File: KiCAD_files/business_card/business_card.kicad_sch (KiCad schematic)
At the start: 80 parts, among them J1 USB_C_Receptacle_USB2.0_14P, J2 Conn_01x05_Pin, SW1 SW_Push, SW2 SW_Push, SW3 SW_Push, SW4 SW_Push, SW5 SW_Push, SW6 SW_Push, SW7 SW_Push, SW8 SW_MEC_5E, U1 STM32U073CCUx, U2 MCP1700x-300xxTT

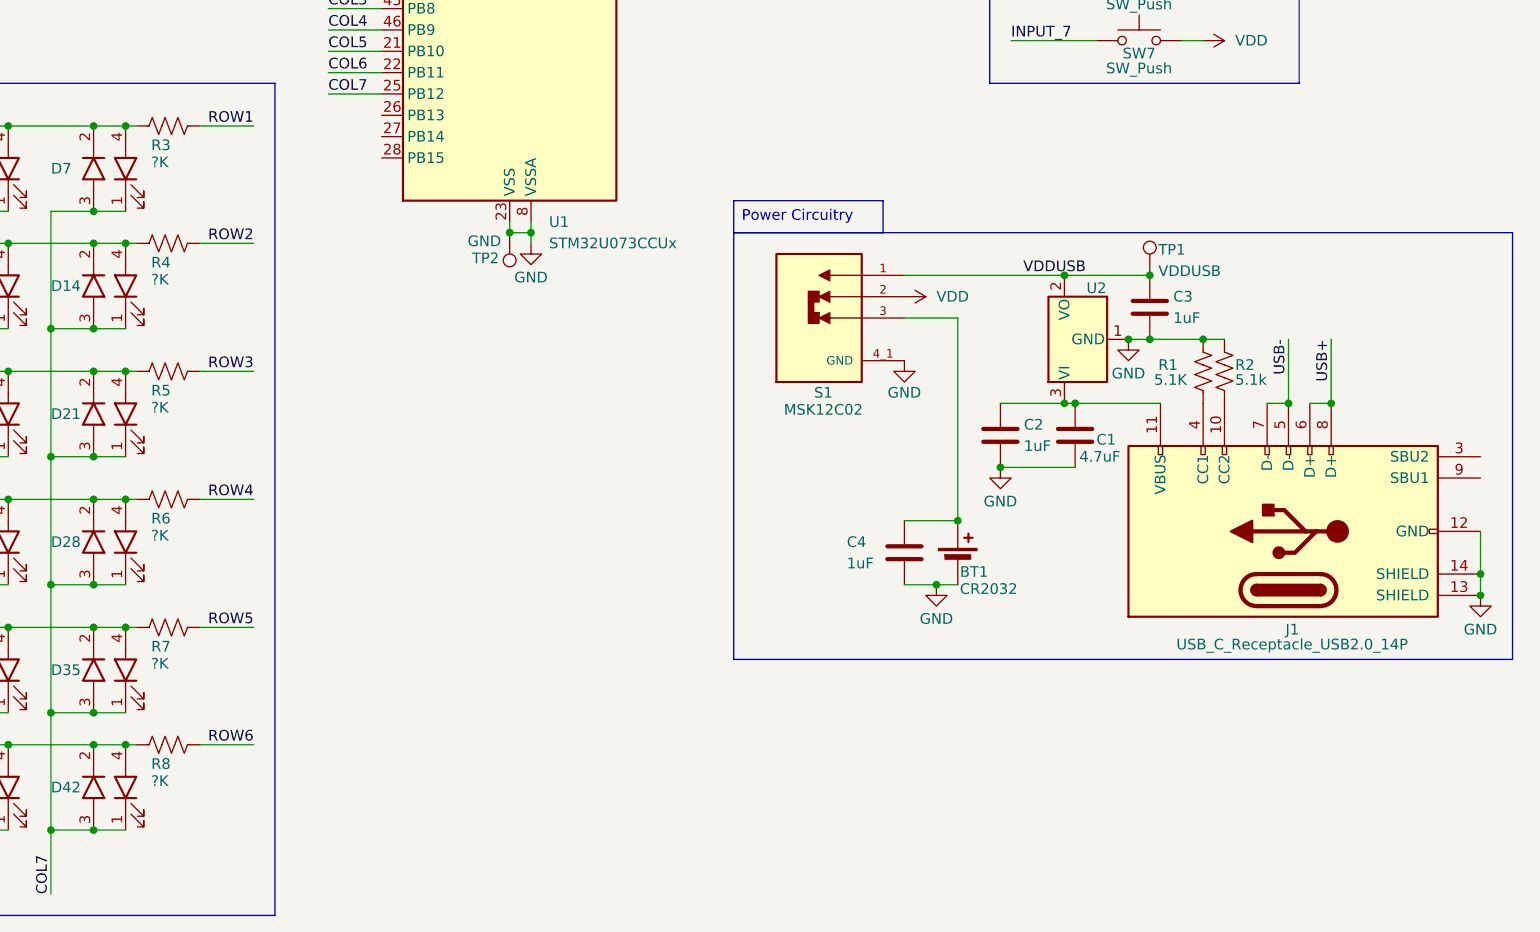
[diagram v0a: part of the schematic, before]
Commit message: Add Contact Info
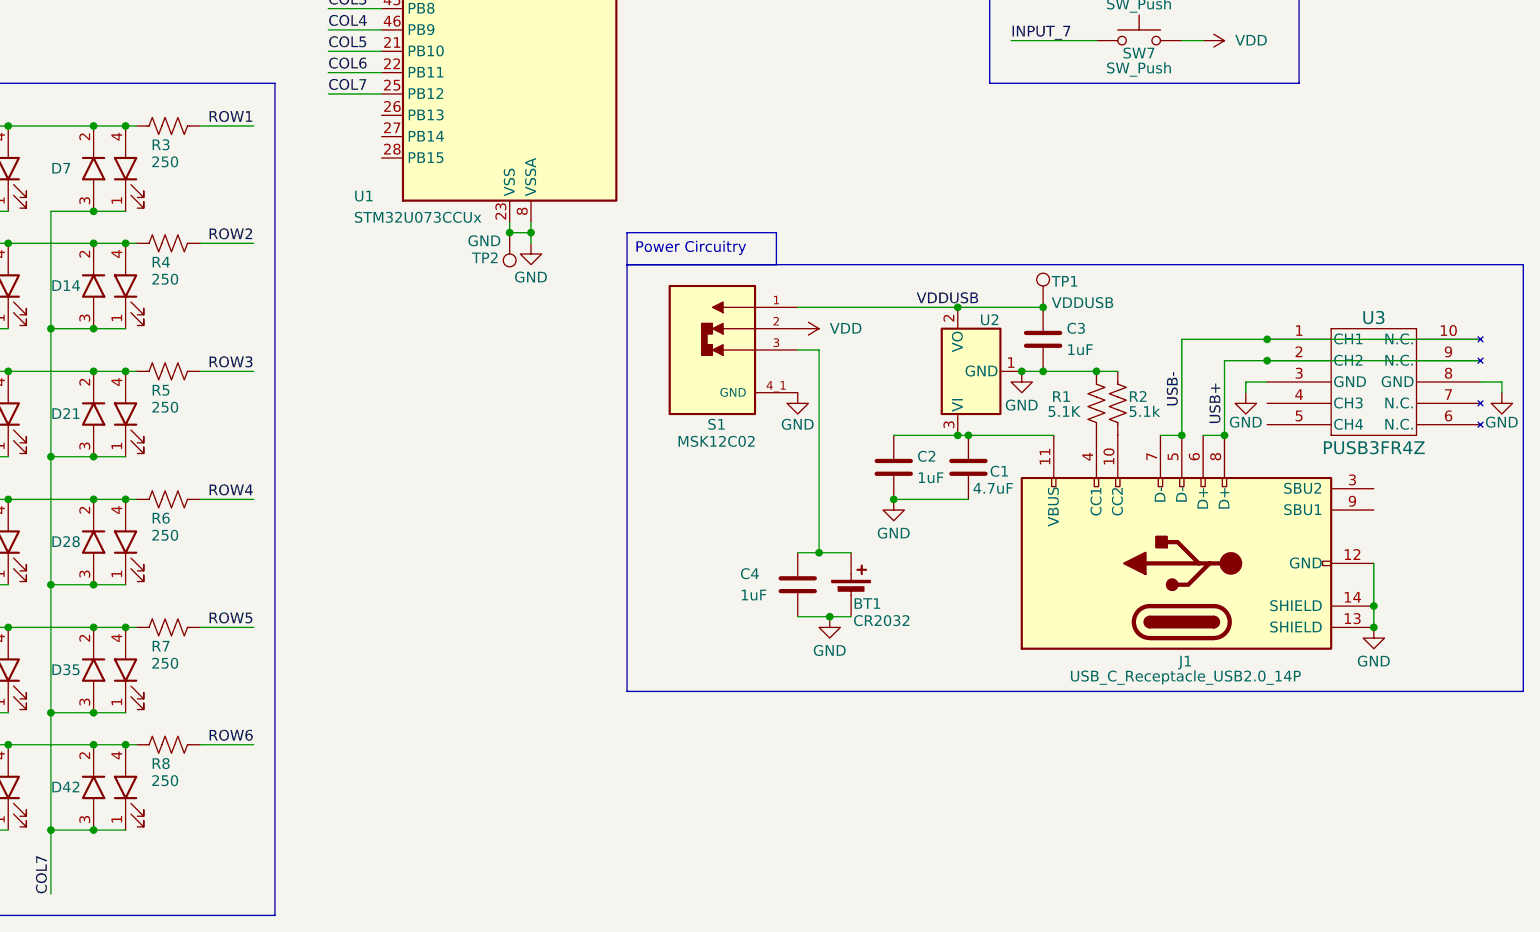
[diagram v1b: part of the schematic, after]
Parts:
- added U3: PUSB3FR4Z, U_PUSB3FR4Z_NEX, symbol ESD_Protection:PUSB3FR4Z
- R3, R4, R5, R6, R7, R8: value ?K -> 250
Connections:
- net GND: now also U3.3 (GND), U3.8 (GND)
- net USB+: now also U3.2 (CH2), U3.9 (N.C.)
- net USB-: now also U3.1 (CH1), U3.10 (N.C.)
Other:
- moved on the sheet: BT1, C1, C2, C3, C4, J1, R1, R2, S1, TP1, U2

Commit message: V1.0 Hardware Production Version Out For Assembly
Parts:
- removed U3: PUSB3FR4Z, U_PUSB3FR4Z_NEX, symbol ESD_Protection:PUSB3FR4Z
- added H1: MountingHole, MountingHole:ToolingHole_1.152mm, symbol Mechanical:MountingHole
- D1, D10, D11, D12, D13, D14, D15, D16, D17, D18, D19, D2, D20, D21, D22, D23, D24, D25, D26, D27, D28, D29, D3, D30, D31, D32, D33, D34, D35, D36, D37, D38, D39, D4, D40, D41, D42, D5, D6, D7, D8, D9: value ~ -> (none)
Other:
- moved on the sheet: BT1, C1, C2, C3, C4, J1, R1, R2, S1, TP1, U2

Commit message: Initial Schematic for V2.0
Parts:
- removed C1: 4.7uF, Capacitor_SMD:C_0603_1608Metric, symbol Device:C
- removed C3: 1uF, Capacitor_SMD:C_0603_1608Metric, symbol Device:C
- removed D1, D10, D11, D12, D13, D14, D15, D16, D17, D18, D19, D2, D20, D21, D22, D23, D24, D25, D26, D27, D28, D29, D3, D30, D31, D32, D33, D34, D35, D36, D37, D38, D39, D4, D40, D41, D42, D5, D6, D7, D8, D9: (no value), P4-1615ROTCA1-0.6T_same_size:LED_CHIP, symbol custom_symbols:P4-1615ROTCA1-0.6T
- removed J1: USB_C_Receptacle_USB2.0_14P, USB-C-SMD_TYPE-C-6PIN-2MD-073:USB-C-SMD_TYPE-C-6PIN-2MD-073, symbol Connector:USB_C_Receptacle_USB2.0_14P
- removed R2: 5.1k, Resistor_SMD:R_0603_1608Metric, symbol Device:R_US
- removed S1: MSK12C02, MSK12C02:SW_MSK12C02, symbol MSK12C02:MSK12C02
- removed SW4, SW5, SW6, SW7: SW_Push, TSB008A2526A:TSB008A2526A, symbol Switch:SW_Push
- removed SW8: SW_MEC_5E, 1TS026A-2000-0553-CT:SW-SMD_4P-L2.6-W1.6-P0.75-LS3.0, symbol Switch:SW_MEC_5E
- removed U1: STM32U073CCUx, Package_DFN_QFN:QFN-48-1EP_7x7mm_P0.5mm_EP5.6x5.6mm, symbol MCU_ST_STM32U0:STM32U073CCUx
- removed U2: MCP1700x-300xxTT, Package_TO_SOT_SMD:SOT-23, symbol Regulator_Linear:MCP1700x-300xxTT
- added D1, D11, D13, D15, D17, D19, D21, D23, D25, D27, D29, D3, D31, D33, D35, D37, D39, D41, D43, D45, D47, D49, D5, D51, D53, D55, D57, D59, D61, D63, D65, D67, D69, D7, D71, D73, D75, D77, D79, D81, D83, D9: RED, LED_SMD:LED_0603_1608Metric, symbol Device:LED
- added D10, D12, D14, D16, D18, D2, D20, D22, D24, D26, D28, D30, D32, D34, D36, D38, D4, D40, D42, D44, D46, D48, D50, D52, D54, D56, D58, D6, D60, D62, D64, D66, D68, D70, D72, D74, D76, D78, D8, D80, D82, D84: ORN, LED_SMD:LED_0603_1608Metric, symbol Device:LED
- added H2: MountingHole, MountingHole:ToolingHole_1.152mm, symbol Mechanical:MountingHole
- added Q1: PMOS, symbol Simulation_SPICE:PMOS
- added R9: 10K, Resistor_SMD:R_0603_1608Metric, symbol Device:R_US
- added TP4: SCL, TestPoint:TestPoint_THTPad_D1.0mm_Drill0.5mm, symbol Connector:TestPoint
- added U1: STM32U073CBTx, Package_QFP:LQFP-48_7x7mm_P0.5mm, symbol MCU_ST_STM32U0:STM32U073CBTx
- added U2: ST25DV04KC-IE6S3, SO-8_STM, symbol 2026-05-02_23-29-46:ST25DV04KC-IE6S3
- C1: renamed from C4; value 1uF -> 47uF
- C2: value 1uF -> 100nF
- R1: value 5.1K -> 10K
- TP1: value VDDUSB -> VDD
- TP3: value VDD -> SDA
- renumbered C10 to C3, C9 to C4, C8 to C5, C11 to C6, C6 to C8, C5 to C9, R9 to R2
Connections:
- net VDDUSB is gone; now on net VDD: R10.1, TP1.1
- net COL1: now also D1.1 (K), D15.1 (K), D16.2 (A), D2.2 (A), D29.1 (K), D30.2 (A), D43.1 (K), D44.2 (A), D57.1 (K), D58.2 (A), D71.1 (K), D72.2 (A), U1.42 (PB6)
- net COL2: now also D17.1 (K), D18.2 (A), D3.1 (K), D31.1 (K), D32.2 (A), D4.2 (A), D45.1 (K), D46.2 (A), D59.1 (K), D60.2 (A), D73.1 (K), D74.2 (A), U1.43 (PB7)
- net COL3: now also D19.1 (K), D20.2 (A), D33.1 (K), D34.2 (A), D47.1 (K), D48.2 (A), D5.1 (K), D6.2 (A), D61.1 (K), D62.2 (A), D75.1 (K), D76.2 (A), U1.45 (PB8)
- net COL4: now also D21.1 (K), D22.2 (A), D35.1 (K), D36.2 (A), D49.1 (K), D50.2 (A), D63.1 (K), D64.2 (A), D7.1 (K), D77.1 (K), D78.2 (A), D8.2 (A), U1.46 (PB9)
- net COL5: now also D10.2 (A), D23.1 (K), D24.2 (A), D37.1 (K), D38.2 (A), D51.1 (K), D52.2 (A), D65.1 (K), D66.2 (A), D79.1 (K), D80.2 (A), D9.1 (K), U1.21 (PB10)
- net COL6: now also D11.1 (K), D12.2 (A), D26.2 (A), D39.1 (K), D40.2 (A), D53.1 (K), D54.2 (A), D67.1 (K), D68.2 (A), D81.1 (K), D82.2 (A), U1.22 (PB11)
- net COL7: now also D13.1 (K), D14.2 (A), D27.1 (K), D28.2 (A), D41.1 (K), D42.2 (A), D55.1 (K), D56.2 (A), D69.1 (K), D70.2 (A), D83.1 (K), D84.2 (A), U1.25 (PB12)
- net GND: now also Q1.2 (G), U1.23 (VSS), U1.35 (VSS), U1.47 (VSS), U1.8 (VSSA), U2.4 (VSS); no longer R1.1
- net NRST: now also R1.2, U1.7 (PF2)
- net ROW1: now also U1.41 (PB5)
- net ROW2: now also U1.40 (PB4)
- net ROW3: now also U1.39 (PB3)
- net ROW4: now also U1.20 (PB2)
- net ROW5: now also U1.19 (PB1)
- net ROW6: now also U1.18 (PB0)
- net SWCLK: now also U1.37 (PA14)
- net SWDIO: now also U1.34 (PA13)
- net VDD: now also C1.1, C2.1, R1.1, Q1.3 (S), R9.1, U1.1 (VBAT), U1.24 (VDD), U1.36 (VDDUSB), U1.48 (VDD), U1.9 (VDDA), U2.8 (VCC); no longer TP3.1
- net at R4.1: now also D15.2 (A), D16.1 (K), D17.2 (A), D18.1 (K), D19.2 (A), D20.1 (K), D21.2 (A), D22.1 (K), D23.2 (A), D24.1 (K), D25.2 (A), D26.1 (K), D27.2 (A), D28.1 (K)
- net at R6.1: now also D43.2 (A), D44.1 (K), D45.2 (A), D46.1 (K), D47.2 (A), D48.1 (K), D49.2 (A), D50.1 (K), D51.2 (A), D52.1 (K), D53.2 (A), D54.1 (K), D55.2 (A), D56.1 (K)
- net at R8.1: now also D71.2 (A), D72.1 (K), D73.2 (A), D74.1 (K), D75.2 (A), D76.1 (K), D77.2 (A), D78.1 (K), D79.2 (A), D80.1 (K), D81.2 (A), D82.1 (K), D83.2 (A), D84.1 (K)
- net at R3.1: now also D1.2 (A), D10.1 (K), D11.2 (A), D12.1 (K), D13.2 (A), D14.1 (K), D2.1 (K), D3.2 (A), D4.1 (K), D5.2 (A), D6.1 (K), D7.2 (A), D8.1 (K), D9.2 (A)
- net at R5.1: now also D29.2 (A), D30.1 (K), D31.2 (A), D32.1 (K), D33.2 (A), D34.1 (K), D35.2 (A), D36.1 (K), D37.2 (A), D38.1 (K), D39.2 (A), D40.1 (K), D41.2 (A), D42.1 (K)
- net at R7.1: now also D57.2 (A), D58.1 (K), D59.2 (A), D60.1 (K), D61.2 (A), D62.1 (K), D63.2 (A), D64.1 (K), D65.2 (A), D66.1 (K), D67.2 (A), D68.1 (K), D69.2 (A), D70.1 (K)
- net NFC_SCL: now reaches R10.2
- net NFC_SCL: now also TP4.1, U1.17 (PA7), U1.30 (PA9), U2.6 (SCL)
- net at R2.1: now also U1.44 (PF3)
- net at BT1.1 (+): now also Q1.1 (D); no longer C1.1
- net INPUT_1 renamed INPUT_DOWN
- net INPUT_DOWN: now also U1.11 (PA1)
- net INPUT_2 renamed INPUT_LEFT
- net INPUT_LEFT: now also U1.12 (PA2)
- net INPUT_3 renamed INPUT_RIGHT
- net INPUT_RIGHT: now also U1.13 (PA3)
- new net: U2.2 (AC0), U2.3 (AC1)
- new net NFC_SDA: R9.2, TP3.1, U1.16 (PA6), U1.31 (PA10), U2.5 (SDA)
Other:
- moved on the sheet: BT1, C1, C3, C4, C5, C6, J2, R2, R3, R4, R5, R6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

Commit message: Initial V2.0 Layout
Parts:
- removed U1: STM32U073CBTx, Package_QFP:LQFP-48_7x7mm_P0.5mm, symbol MCU_ST_STM32U0:STM32U073CBTx
- added U1: STM32U073CCUx, Package_DFN_QFN:QFN-48-1EP_7x7mm_P0.5mm_EP5.6x5.6mm, symbol MCU_ST_STM32U0:STM32U073CCUx
- BT1: footprint Battery:BatteryHolder_Keystone_3002_1x2032 -> BAT_HLD_005_THM:BAT_BAT-HLD-005-THM
- Q1: value PMOS -> AO3401A; footprint (none) -> AO3401A:SOT-23-3L_AOS-L
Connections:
- net COL1: now also U1.42 (PB6)
- net COL2: now also U1.43 (PB7)
- net COL3: now also U1.45 (PB8)
- net COL4: now also U1.46 (PB9)
- net COL5: now also U1.21 (PB10)
- net COL6: now also U1.22 (PB11)
- net COL7: now also U1.25 (PB12)
- net GND: now also U1.23 (VSS), U1.35 (VSS), U1.47 (VSS), U1.49 (VSS), U1.8 (VSSA)
- net INPUT_DOWN: now also U1.11 (PA1)
- net INPUT_LEFT: now also U1.12 (PA2)
- net INPUT_RIGHT: now also U1.13 (PA3)
- net NFC_SCL: now also U1.17 (PA7)
- net NFC_SDA: now also U1.16 (PA6)
- net NRST: now also U1.7 (PF2)
- net ROW1: now also U1.41 (PB5)
- net ROW2: now also U1.40 (PB4)
- net ROW3: now also U1.39 (PB3)
- net ROW4: now also U1.20 (PB2)
- net ROW5: now also U1.19 (PB1)
- net ROW6: now also U1.18 (PB0)
- net SWCLK: now also U1.37 (PA14)
- net SWDIO: now also U1.34 (PA13)
- net VDD: now also U1.1 (VBAT), U1.24 (VDD), U1.36 (VDDUSB), U1.48 (VDD), U1.9 (VDDA)
- net L = 5.634 uH: now reaches U2.2 (AC0), U2.3 (AC1)
- net at R2.1: now also U1.44 (PF3)
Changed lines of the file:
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@@
 	(wire
 		(pts
-			(xy 176.53 81.28) (xy 186.69 81.28)
-		)
-		(stroke
-			(width 0)
-			(type default)
-		)
-	)
-	(wire
-		(pts
 			(xy 53.34 171.45) (xy 53.34 172.72)
 		)
@@
 	(wire
 		(pts
-			(xy 176.53 83.82) (xy 186.69 83.82)
-		)
-		(stroke
-			(width 0)
-			(type default)
-		)
-	)
-	(wire
-		(pts
 			(xy 34.29 181.61) (xy 34.29 168.91)
 		)
@@
 		)
 	)
-	(label "NFC_SDA"
-		(at 186.69 83.82 180)
-		(effects
-			(font
-				(size 1.27 1.27)
-			)
-			(justify right bottom)
-		)
-	)
 	(label "ROW3"
 		(at 139.7 88.9 0)
@@
 		)
 	)
-	(label "NFC_SCL"
-		(at 186.69 81.28 180)
+	(label "L = 5.634 uH"
+		(at 205.74 130.81 0)
 		(effects
 			(font
 				(size 1.27 1.27)
 			)
-			(justify right bottom)
+			(justify left bottom)
 		)
 	)
@@
 			)
 		)
-		(property "Footprint" "Battery:BatteryHolder_Keystone_3002_1x2032"
+		(property "Footprint" "BAT_HLD_005_THM:BAT_BAT-HLD-005-THM"
 			(at 227.33 89.916 90)
 			(hide yes)
@@
 	)
 	(symbol
+		(lib_id "MCU_ST_STM32U0:STM32U073CCUx")
+		(at 161.29 88.9 0)
+		(unit 1)
+		(body_style 1)
+		(exclude_from_sim no)
+		(in_bom yes)
+		(on_board yes)
+		(in_pos_files yes)
+		(dnp no)
+		(fields_autoplaced yes)
+		(property "Reference" "U1"
+			(at 165.9733 127 0)
+			(show_name no)
+			(do_not_autoplace no)
+			(effects
+				(font
+					(size 1.27 1.27)
+				)
+				(justify left)
+			)
+		)
+		(property "Value" "STM32U073CCUx"
+			(at 165.9733 129.54 0)
+			(show_name no)
+			(do_not_autoplace no)
+			(effects
+				(font
+					(size 1.27 1.27)
+				)
+				(justify left)
+			)
+		)
+		(property "Footprint" "Package_DFN_QFN:QFN-48-1EP_7x7mm_P0.5mm_EP5.6x5.6mm"
+			(at 148.59 124.46 0)
+			(hide yes)
+			(show_name no)
+			(do_not_autoplace no)
+			(effects
+				(font
+					(size 1.27 1.27)
+				)
+				(justify right)
+			)
+		)
+		(property "Datasheet" "https://www.st.com/resource/en/datasheet/stm32u073cc.pdf"
+			(at 161.29 88.9 0)
+			(hide yes)
+			(show_name no)
+			(do_not_autoplace no)
+			(effects
+				(font
+					(size 1.27 1.27)
+				)
+			)
+		)
+		(property "Description" "STMicroelectronics Arm Cortex-M0+ MCU, 256KB flash, 40KB RAM, 56 MHz, 39 GPIO, UFQFPN48"
+			(at 161.29 88.9 0)
+			(hide yes)
+			(show_name no)
+			(do_not_autoplace no)
+			(effects
+				(font
+					(size 1.27 1.27)
+				)
+			)
+		)
+		(pin "14"
+		)
+		(pin "24"
+		)
+		(pin "26"
+		)
+		(pin "5"
+		)
+		(pin "7"
+		)
+		(pin "6"
+		)
+		(pin "19"
+		)
+		(pin "15"
+		)
+		(pin "16"
+		)
+		(pin "2"
+		)
+		(pin "3"
+		)
+		(pin "18"
+		)
+		(pin "22"
+		)
+		(pin "4"
+		)
+		(pin "9"
+		)
+		(pin "11"
+		)
+		(pin "13"
+		)
+		(pin "12"
+		)
+		(pin "17"
+		)
+		(pin "20"
+		)
+		(pin "8"
+		)
+		(pin "21"
+		)
+		(pin "1"
+		)
+		(pin "10"
+		)
+		(pin "23"
+		)
+		(pin "25"
+		)
+		(pin "42"
+		)
+		(pin "40"
+		)
+		(pin "45"
+		)
+		(pin "34"
+		)
+		(pin "36"
+		)
+		(pin "37"
+		)
+		(pin "46"
+		)
+		(pin "39"
+		)
+		(pin "48"
+		)
+		(pin "31"
+		)
+		(pin "30"
+		)
+		(pin "33"
+		)
+		(pin "35"
+		)
+		(pin "43"
+		)
+		(pin "44"
+		)
+		(pin "28"
+		)
+		(pin "29"
+		)
+		(pin "32"
+		)
+		(pin "27"
+		)
+		(pin "38"
+		)
+		(pin "41"
+		)
+		(pin "49"
+		)
+		(pin "47"
+		)
+		(instances
+			(project "business_card"
+				(path "/16d1a3fe-4f2d-4eb3-9740-21c0af2e4feb"
+					(reference "U1")
+					(unit 1)
+				)
+			)
+		)
+	)
+	(symbol
 		(lib_id "Device:LED")
 		(at 109.22 151.13 90)
@@
 	)
 	(symbol
-		(lib_id "MCU_ST_STM32U0:STM32U073CBTx")
-		(at 161.29 88.9 0)
-		(unit 1)
-		(body_style 1)
-		(exclude_from_sim no)
-		(in_bom yes)
-		(on_board yes)
-		(in_pos_files yes)
-		(dnp no)
-		(fields_autoplaced yes)
-		(property "Reference" "U1"
-			(at 165.9733 127 0)
-			(show_name no)
-			(do_not_autoplace no)
-			(effects
-				(font
-					(size 1.27 1.27)
-				)
-				(justify left)
-			)
-		)
-		(property "Value" "STM32U073CBTx"
-			(at 165.9733 129.54 0)
-			(show_name no)
-			(do_not_autoplace no)
-			(effects
-				(font
-					(size 1.27 1.27)
-				)
-				(justify left)
-			)
-		)
-		(property "Footprint" "Package_QFP:LQFP-48_7x7mm_P0.5mm"
-			(at 148.59 124.46 0)
-			(hide yes)
-			(show_name no)
-			(do_not_autoplace no)
-			(effects
-				(font
-					(size 1.27 1.27)
-				)
-				(justify right)
-			)
-		)
-		(property "Datasheet" "https://www.st.com/resource/en/datasheet/stm32u073cb.pdf"
-			(at 161.29 88.9 0)
-			(hide yes)
-			(show_name no)
-			(do_not_autoplace no)
-			(effects
-				(font
-					(size 1.27 1.27)
-				)
-			)
-		)
-		(property "Description" "STMicroelectronics Arm Cortex-M0+ MCU, 128KB flash, 40KB RAM, 39 GPIO, LQFP48"
-			(at 161.29 88.9 0)
-			(hide yes)
-			(show_name no)
-			(do_not_autoplace no)
-			(effects
-				(font
-					(size 1.27 1.27)
-				)
-			)
-		)
-		(pin "6"
-		)
-		(pin "14"
-		)
-		(pin "19"
-		)
-		(pin "17"
-		)
-		(pin "12"
-		)
-		(pin "13"
-		)
-		(pin "18"
-		)
-		(pin "16"
-		)
-		(pin "22"
-		)
-		(pin "25"
-		)
-		(pin "8"
-		)
-		(pin "2"
-		)
-		(pin "11"
-		)
-		(pin "35"
-		)
-		(pin "7"
-		)
-		(pin "4"
-		)
-		(pin "10"
-		)
-		(pin "3"
-		)
-		(pin "1"
-		)
-		(pin "5"
-		)
-		(pin "9"
-		)
-		(pin "21"
-		)
-		(pin "23"
-		)
-		(pin "28"
-		)
-		(pin "15"
-		)
-		(pin "29"
-		)
-		(pin "30"
-		)
-		(pin "32"
-		)
-		(pin "27"
-		)
-		(pin "33"
-		)
-		(pin "24"
-		)
-		(pin "20"
-		)
-		(pin "26"
-		)
-		(pin "31"
-		)
-		(pin "34"
-		)
-		(pin "48"
-		)
-		(pin "39"
-		)
-		(pin "41"
-		)
-		(pin "44"
-		)
-		(pin "42"
-		)
-		(pin "43"
-		)
-		(pin "46"
-		)
-		(pin "40"
-		)
-		(pin "45"
-		)
-		(pin "47"
-		)
-		(pin "37"
-		)
-		(pin "38"
-		)
-		(pin "36"
-		)
-		(instances
-			(project "business_card"
-				(path "/16d1a3fe-4f2d-4eb3-9740-21c0af2e4feb"
-					(reference "U1")
-					(unit 1)
-				)
-			)
-		)
-	)
-	(symbol
 		(lib_id "Device:LED")
 		(at 71.12 113.03 270)
@@
 			)
 		)
-		(property "Value" "PMOS"
+		(property "Value" "AO3401A"
 			(at 238.76 83.058 90)
 			(show_name no)
@@
 			)
 		)
-		(property "Footprint" ""
+		(property "Footprint" "AO3401A:SOT-23-3L_AOS-L"
 			(at 236.22 83.82 0)
 			(hide yes)
